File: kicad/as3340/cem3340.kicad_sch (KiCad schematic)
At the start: 55 parts

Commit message: kicad library fix...again
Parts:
- C14, C15: renamed from C?; value (none) -> 1u; footprint (none) -> Capacitor_SMD:C_1206_3216Metric
- C17, C18, C19, C23, C33: value (none) -> 10n; footprint (none) -> Capacitor_SMD:C_0603_1608Metric
- C20: value (none) -> 100n; footprint (none) -> Capacitor_SMD:C_0603_1608Metric
- C21: value (none) -> 1000p; footprint (none) -> Capacitor_THT:Nichicon QYX2A102KTP
- C22, C35: value (none) -> 0.1u; footprint (none) -> Capacitor_SMD:C_0603_1608Metric
- D1, D2: renamed from D?; value (none) -> 1N4148W; footprint (none) -> Diode_SMD:D_SOD-123
- R15, R16: value (none) -> 68k; footprint (none) -> Resistor_SMD:R_0603_1608Metric
- R17, R22: value (none) -> 56k; footprint (none) -> Resistor_SMD:R_0603_1608Metric
- R18: value (none) -> 82k; footprint (none) -> Resistor_SMD:R_0603_1608Metric
- R19: value (none) -> 33k; footprint (none) -> Resistor_SMD:R_0603_1608Metric
- R21, R24, R28, R41, R57: value (none) -> 10k; footprint (none) -> Resistor_SMD:R_0603_1608Metric
- R23, R27, R29, R30, R37, R43: value (none) -> 1M; footprint (none) -> Resistor_SMD:R_0603_1608Metric
- R25, R34: value (none) -> 5k6; footprint (none) -> Resistor_SMD:R_0603_1608Metric
- R31: value (none) -> 1.5M; footprint (none) -> Resistor_SMD:R_0603_1608Metric
- R32, R46: value (none) -> 470; footprint (none) -> Resistor_SMD:R_0805_2012Metric
- R33: value (none) -> 20K; footprint (none) -> Resistor_SMD:R_0603_1608Metric
- R35: value (none) -> 1K82; footprint (none) -> Resistor_SMD:R_0603_1608Metric
- R36: value (none) -> 51k; footprint (none) -> Resistor_SMD:R_0603_1608Metric
- R38: value (none) -> 100k 0.1%; footprint (none) -> Resistor_SMD:R_0603_1608Metric
- R42: value (none) -> 300k; footprint (none) -> Resistor_SMD:R_0603_1608Metric
- R44: value (none) -> 18k; footprint (none) -> Resistor_SMD:R_0603_1608Metric
- R45: value (none) -> 13k; footprint (none) -> Resistor_SMD:R_0603_1608Metric
- R58: value (none) -> 220k; footprint (none) -> Resistor_SMD:R_0603_1608Metric
- RV1: value (none) -> 10K; footprint (none) -> Potentiometer_THT:Potentiometer_Bourns_3296W_Vertical
- RV2: value (none) -> 20k; footprint (none) -> Potentiometer_THT:Potentiometer_Bourns_3296W_Vertical
- TP1, TP2, TP4, TP5: value (none) -> TestPoint; footprint (none) -> TestPoint:TestPoint_Pad_2.0x2.0mm
- U10: renamed from U?; value (none) -> LM79L05; footprint (none) -> Package_TO_SOT_THT:TO-92_Inline_Wide
- U11: value (none) -> LM393; footprint (none) -> Package_SO:SOIC-8_3.9x4.9mm_P1.27mm
- U2: value (none) -> TL074; footprint (none) -> Package_SO:SOIC-14_3.9x8.7mm_P1.27mm
- U3: value (none) -> AS3340; footprint (none) -> Package_SO:SOIC-16_3.9x9.9mm_P1.27mm
- U8, U9: value (none) -> DG442CY+; footprint (none) -> Package_SO:SOIC-16_3.9x9.9mm_P1.27mm

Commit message: remove rescue library
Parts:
- RV1, RV2: symbol as3340-rescue:R_POT_TRIM-Device -> as3340:R_POT_TRIM-Device
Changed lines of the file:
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@@
     (pin "2")
   )
-  (symbol (lib_id "as3340-rescue:R_POT_TRIM-Device") (at 222.25 165.1 0) (unit 1)
+  (symbol (lib_id "as3340:R_POT_TRIM-Device") (at 222.25 165.1 0) (unit 1)
     (in_bom yes) (on_board yes)
     (property "Reference" "RV1" (id 0) (at 220.4974 163.9316 0)
@@
     (pin "2")
   )
-  (symbol (lib_id "as3340-rescue:R_POT_TRIM-Device") (at 317.5 31.75 0) (unit 1)
+  (symbol (lib_id "as3340:R_POT_TRIM-Device") (at 317.5 31.75 0) (unit 1)
     (in_bom yes) (on_board yes)
     (property "Reference" "RV2" (id 0) (at 315.722 30.5816 0)

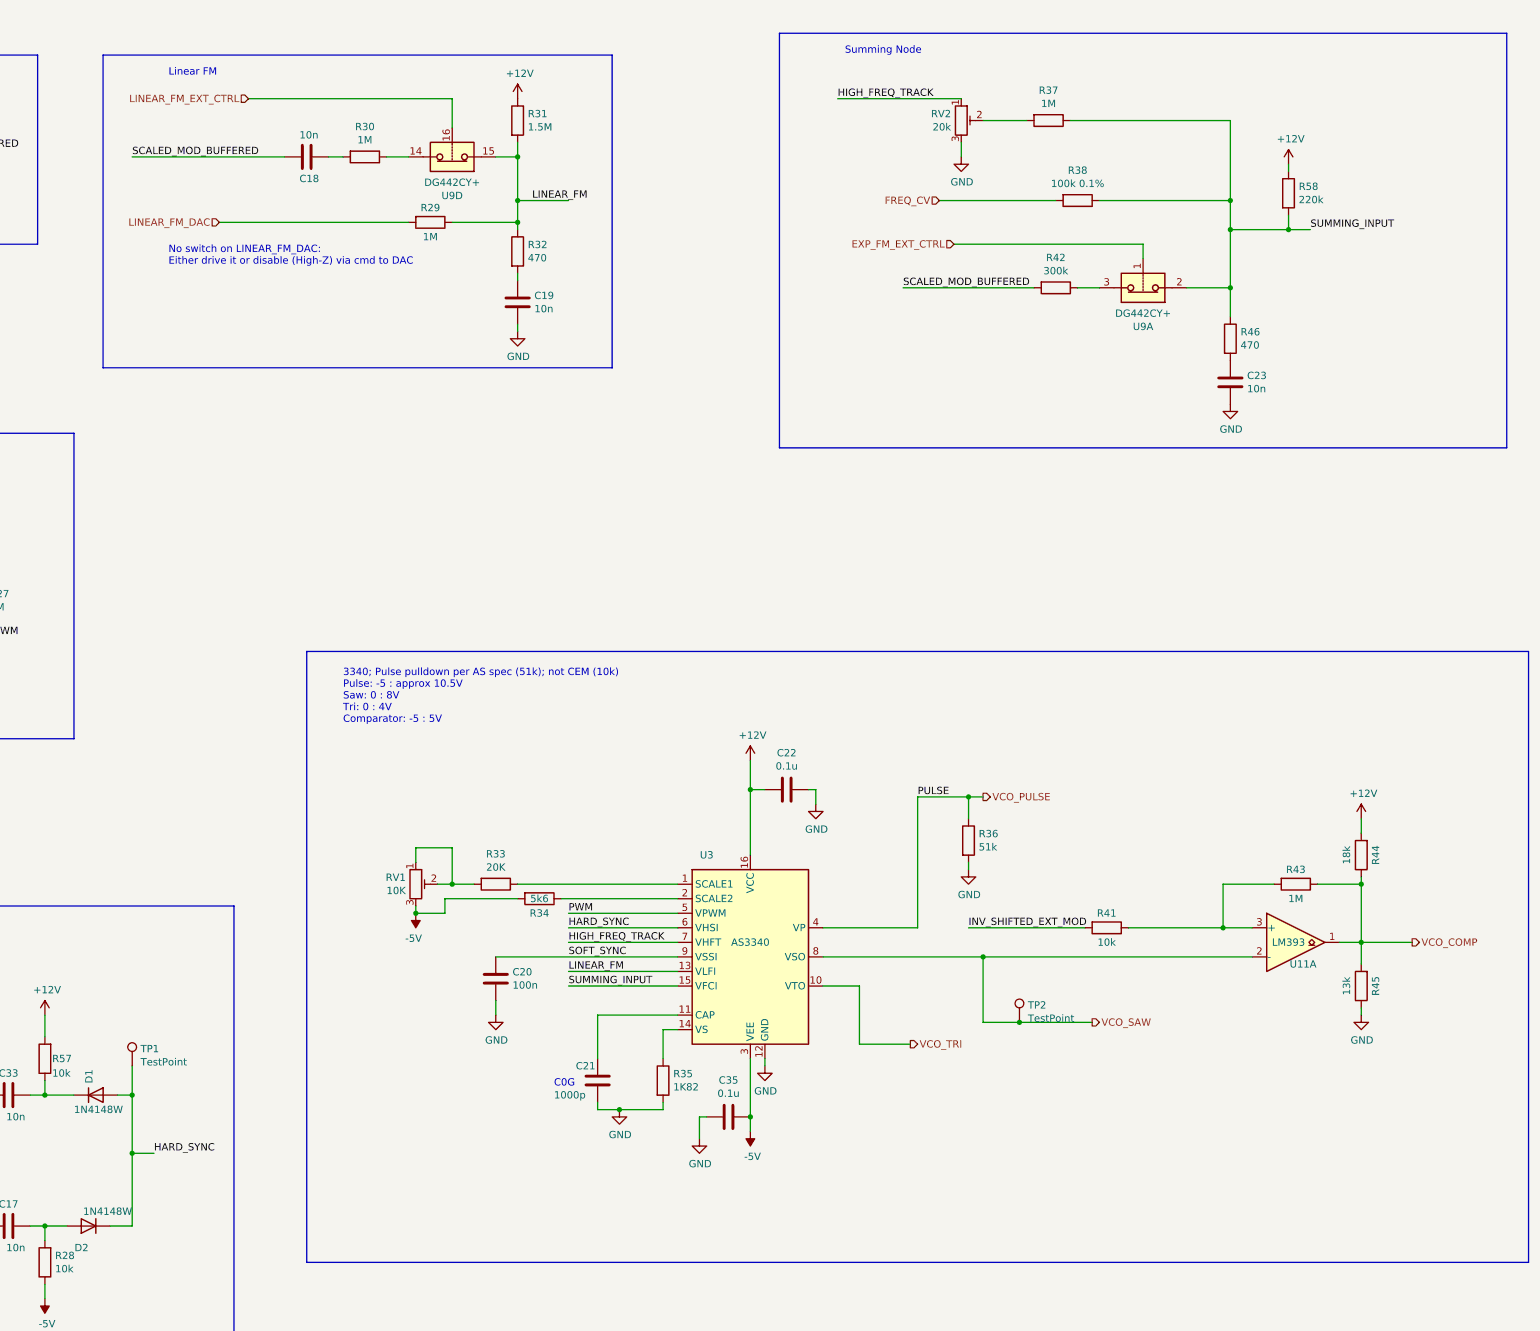
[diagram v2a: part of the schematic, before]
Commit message: modify tuning to 4 trimmer method
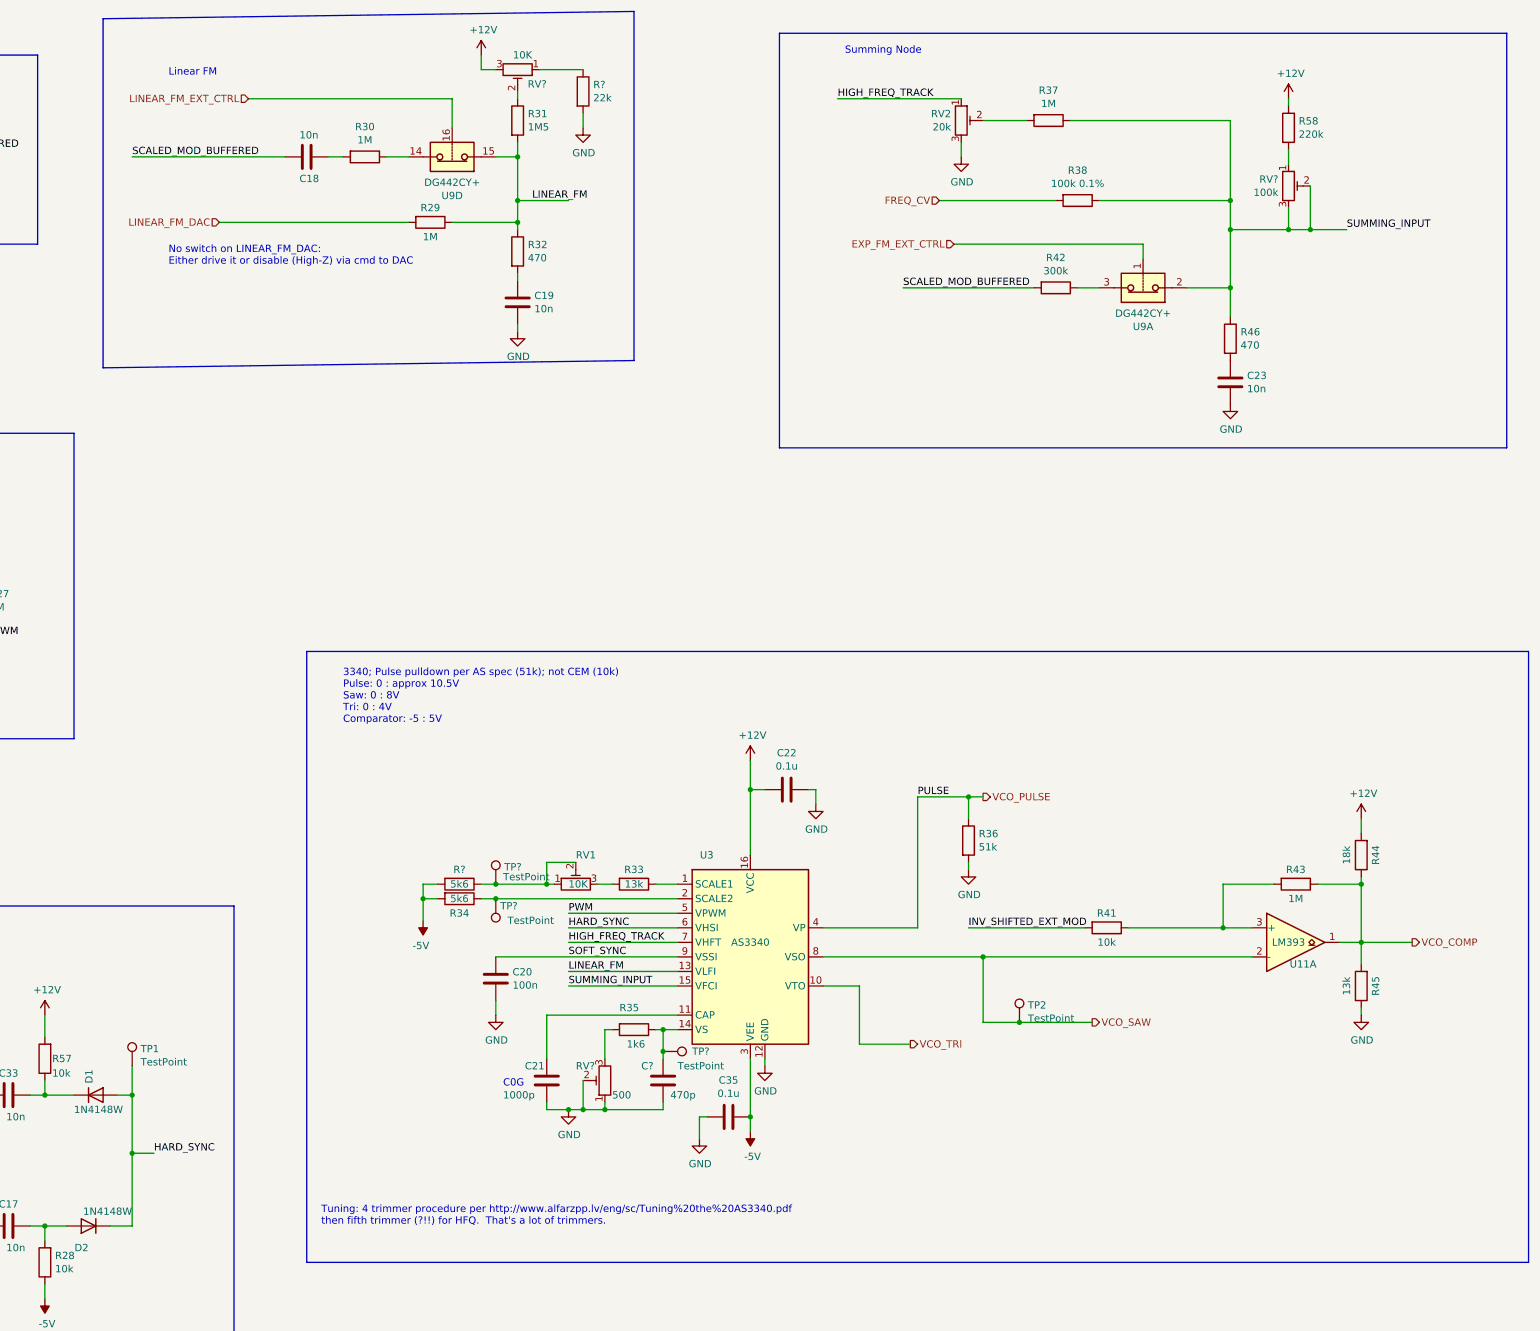
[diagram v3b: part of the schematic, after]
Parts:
- added C?: 470p, Capacitor_SMD:C_0603_1608Metric, symbol Device:C
- added R?: 5k6, Resistor_SMD:R_0603_1608Metric, symbol Device:R
- added R?: 22k, Resistor_SMD:R_0603_1608Metric, symbol Device:R
- added RV?: 100k, Potentiometer_THT:Potentiometer_Bourns_3296W_Vertical, symbol as3340:R_POT_TRIM-Device
- added RV?: 10K, Potentiometer_THT:Potentiometer_Bourns_3296W_Vertical, symbol as3340:R_POT_TRIM-Device
- added RV?: 500, Potentiometer_THT:Potentiometer_Bourns_3296W_Vertical, symbol as3340:R_POT_TRIM-Device
- added TP? (x3): TestPoint, TestPoint:TestPoint_Pad_2.0x2.0mm, symbol Connector:TestPoint
- R31: value 1.5M -> 1M5
- R33: value 20K -> 13k; LCSC Part C4184 -> C22797
- R35: value 1K82 -> 1k6; LCSC Part C4177 -> C22847
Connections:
- net +12V: now also RV?.3; no longer R31.1
- net -5V: now also R?.2; no longer RV1.3
- net GND: now also C?.2, R?.2, RV?.1, RV?.2; no longer R35.2
- net SUMMING_INPUT: now also RV?.2, RV?.3; no longer R58.2
- net at R35.1, U3.14 (VS): now also C?.1, TP?.1
- net at R34.1, U3.2 (SCALE2): now also TP?.1
- net at RV1.1, RV1.2: now also R?.1, TP?.1; no longer R33.2
- new net: R33.2, RV1.3
- new net: R31.1, RV?.2
- new net: R35.2, RV?.3
- new net: R58.2, RV?.1
- new net: R?.1, RV?.1
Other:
- note added: "3340; Pulse pulldown per AS spec (51k); not CEM (10k) Pulse: 0 : approx 10.5V Saw: 0 : 8V Tri: 0 : 4V Comparator: -5 : 5V"
- note added: "Tuning: 4 trimmer procedure per http://www.alfarzpp.lv/eng/sc/Tuning%20the%20AS3340.pdf then fifth trimmer (?!!) for HFQ. That's a lot of trimmers."
- note removed: "3340; Pulse pulldown per AS spec (51k); not CEM (10k) Pulse: -5 : approx 10.5V Saw: 0 : 8V Tri: 0 : 4V Comparator: -5 : 5V"
- moved on the sheet: C21, R33, R34, R35, R58, RV1

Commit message: schematic changes, still need values
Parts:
- R42: value 300k -> 200k; LCSC Part C23024 -> C25811
- R58: value 220k -> 200k; LCSC Part C22961 -> (none)
- gave numbers to parts that had none: 9
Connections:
- net +12V: now also RV5.1, RV5.2; no longer R58.1
- net SUMMING_INPUT: now also R58.2; no longer RV5.2, RV5.3
- new net: R58.1, RV5.3
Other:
- note added: "Hard Sync Selection and Control OSC_EXTERNAL: assume somewhere around +/- 5V but it could well be outside that; attenuate/invert external to 0-5V for both 393 comparators; keep external signal inside -5 : +12 inv_shifted_ext_mod = osc_external * 0.5 + 2.5"
- note added: "PWM control is 0 - 5V per datasheet at +15 V supply. Specifically, it’s zero to Sawtooth level / 2; for +12V: 0 - 4V"
- note added: "Summing Node / Exponential Frequency"
- note removed: "Hard Sync Selection and Control OSC_EXTERNAL: assume somewhere around +/- 5V but it could well be outside that; attenuate/invert external to 0-5V for both 393 comparators; keep external signal inside -5 : +12"
- note removed: "PWM control is 0 - 5V per datasheet at +15 V supply. Specifically, it’s zero to Sawtooth level / 2, so 0 - 4V w/ +12"
- note removed: "Summing Node"
- moved on the sheet: R58, RV5
